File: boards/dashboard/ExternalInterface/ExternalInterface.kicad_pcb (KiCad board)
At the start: 2 copper layers, 85.2 x 44.4 mm, 4 parts, among them J1 micromatch_female_TOP_ENTRY_l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, J2 Ampseal_14, J3 micromatch_female_TOP_ENTRY_l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, U1 RJ45_VT

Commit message: Gerbers and PDFs
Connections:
- J2 pad 1: Net-(J2-Pad1) -> GND
- J2 pad 10: Net-(J2-Pad10) -> CANH
- J2 pad 11: Net-(J2-Pad11) -> CANL
- J2 pad 12: GND -> +12V
- J2 pad 13: +12V -> Net-(J2-Pad13)
- J2 pad 14: GND -> Net-(J2-Pad14)
- J2 pad 2: Net-(J2-Pad2) -> GND
- J2 pad 3: CANL -> GND
- J2 pad 4: CANH -> Net-(J2-Pad4)
- J2 pad 5: GND -> Net-(J2-Pad5)
- J2 pad 6: Net-(J2-Pad6) -> CANH
- J2 pad 8: CANH -> +12V
- J2 pad 9: +12V -> Net-(J2-Pad9)
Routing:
- net +12V: track 58.6 -> 40.5 mm, vias 0 -> 1
- net VCC: track 69.9 -> 79.2 mm, vias 2 -> 0
- net CANH: track 74.2 -> 77.2 mm, vias 1 -> 0
- net LED1: track 85.1 -> 82.1 mm, vias 2 -> 0
- net CANL: track 80.9 -> 78.2 mm
- net AT_RESET: track 71.9 -> 74.3 mm
- net SCK: track 72.7 -> 75.0 mm
- net LED2: track 70.3 -> 68.0 mm, vias 2 -> 0
- net MISO: track 74.4 -> 76.3 mm
- net MOSI: track 75.7 -> 77.1 mm

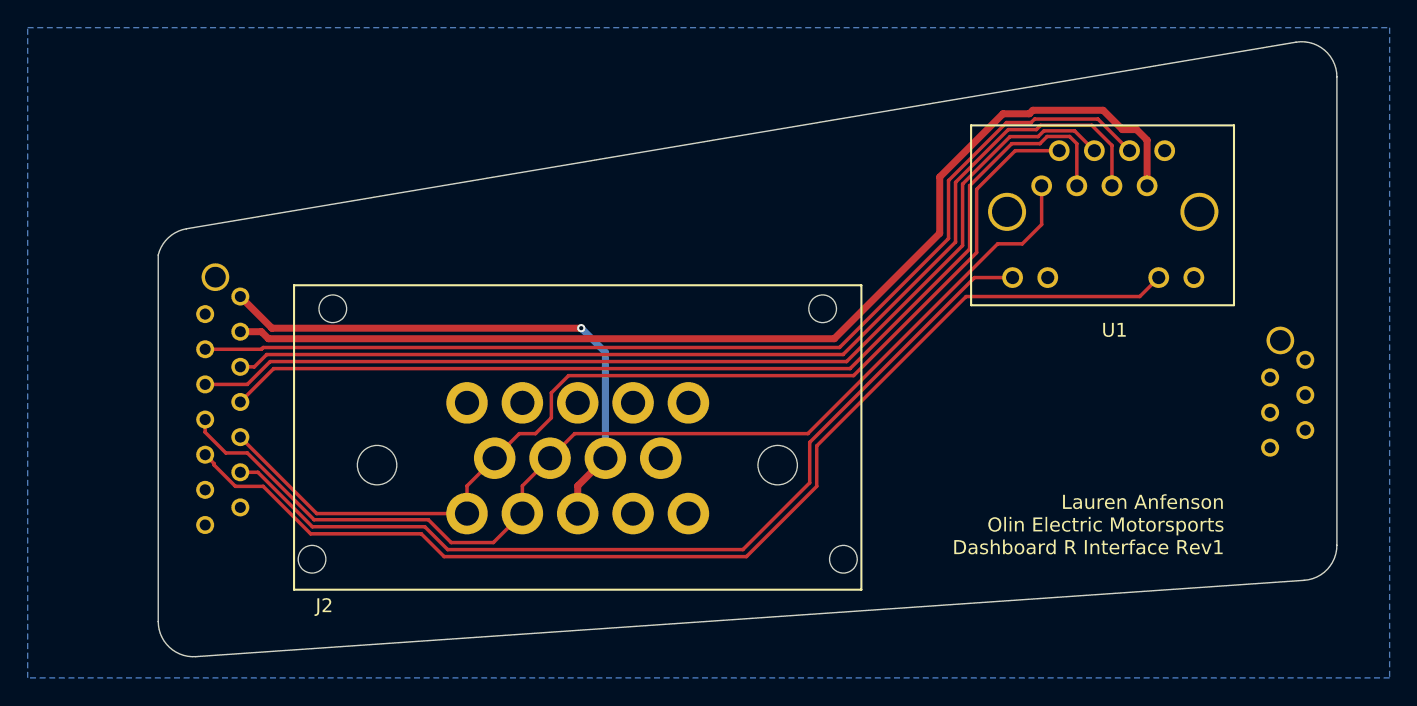
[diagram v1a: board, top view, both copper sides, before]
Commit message: Updated External Interface
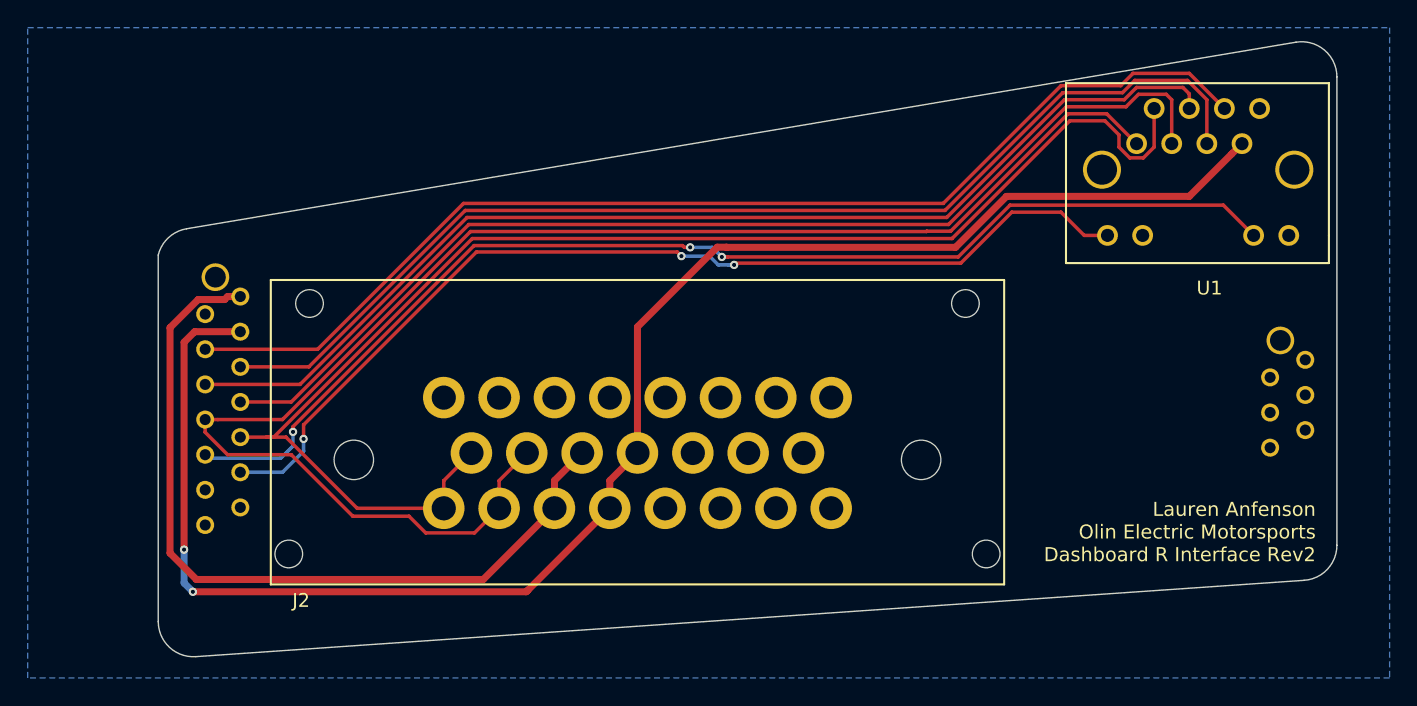
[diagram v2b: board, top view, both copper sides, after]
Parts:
- J2: value Ampseal_14 -> Ampseal_23; footprint footprints:Ampseal_14 -> footprints:Ampseal_23
- moved U1 7.50 mm to (165.0, 70.9)
- moved J2 1.72 mm to (110.6, 87.1)
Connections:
- J2 pad 10: CANH -> CANL
- J2 pad 11: CANL -> +12V
- J2 pad 12: +12V -> VCC
- J2 pad 3: GND -> Net-(J2-Pad3)
- J2 pad 5: Net-(J2-Pad5) -> GND
- J2 pad 6: CANH -> Net-(J2-Pad6)
- J2 pad 7: CANL -> Net-(J2-Pad7)
- J2 pad 8: +12V -> Net-(J2-Pad8)
- J2 pad 9: Net-(J2-Pad9) -> CANH
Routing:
- net VCC: track 79.2 -> 118.4 mm, vias 0 -> 2
- net CANL: track 78.2 -> 108.1 mm
- net CANH: track 77.2 -> 100.0 mm
- net +12V: track 40.5 -> 57.8 mm, vias 1 -> 0
- net SCK: track 75.0 -> 81.3 mm
- net MISO: track 76.3 -> 82.2 mm
- net MOSI: track 77.1 -> 83.0 mm
- net AT_RESET: track 74.3 -> 79.9 mm
- net LED2: track 68.0 -> 73.0 mm, vias 0 -> 3
- net LED1: track 82.1 -> 85.9 mm, vias 0 -> 3
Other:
- board text added: "Lauren Anfenson Olin Electric Motorsports Dashboard R Interface Rev2"
- board text removed: "Lauren Anfenson Olin Electric Motorsports Dashboard R Interface Rev1"
